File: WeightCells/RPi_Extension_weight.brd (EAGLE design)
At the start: 80 x 50 mm, 29 parts, among them U1 AD7730BRUZ, U2 AD7730BRUZ, U3 AD7730BRUZ, U4 AD7730BRUZ, U5 AD7730BRUZ, U6 AD7730BRUZ, U7 AD7730BRUZ, U8 AD7730BRUZ, U9 STM32F103RCT6

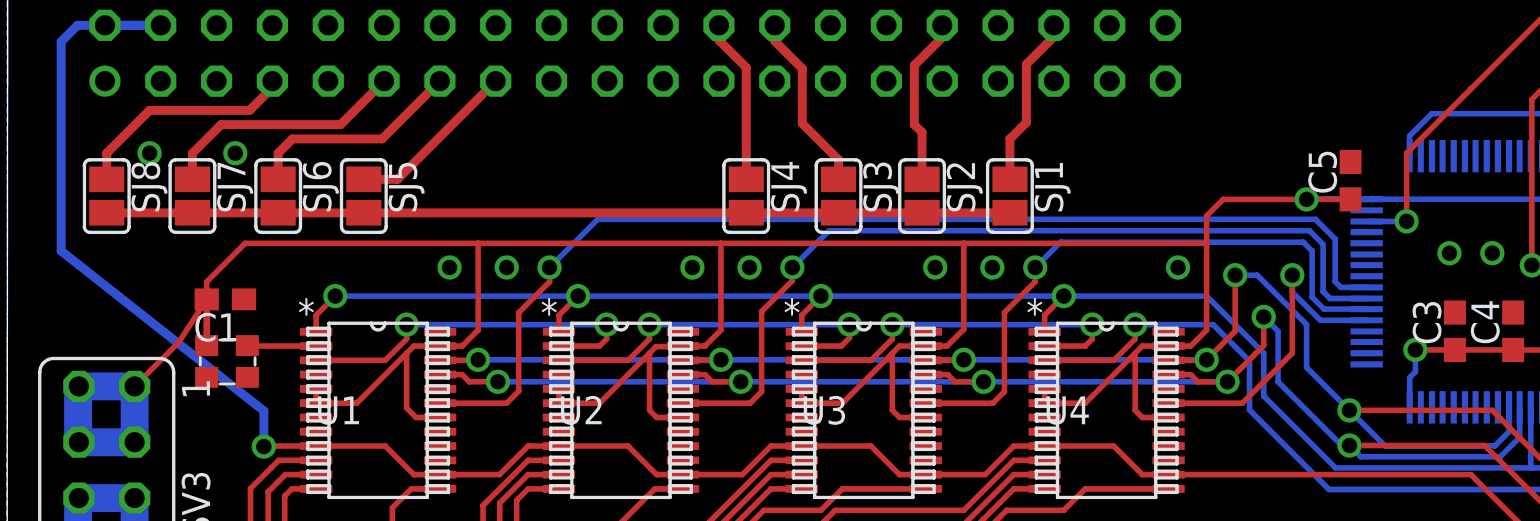
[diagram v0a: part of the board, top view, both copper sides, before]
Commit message: fixed grounding error and missplaced trace
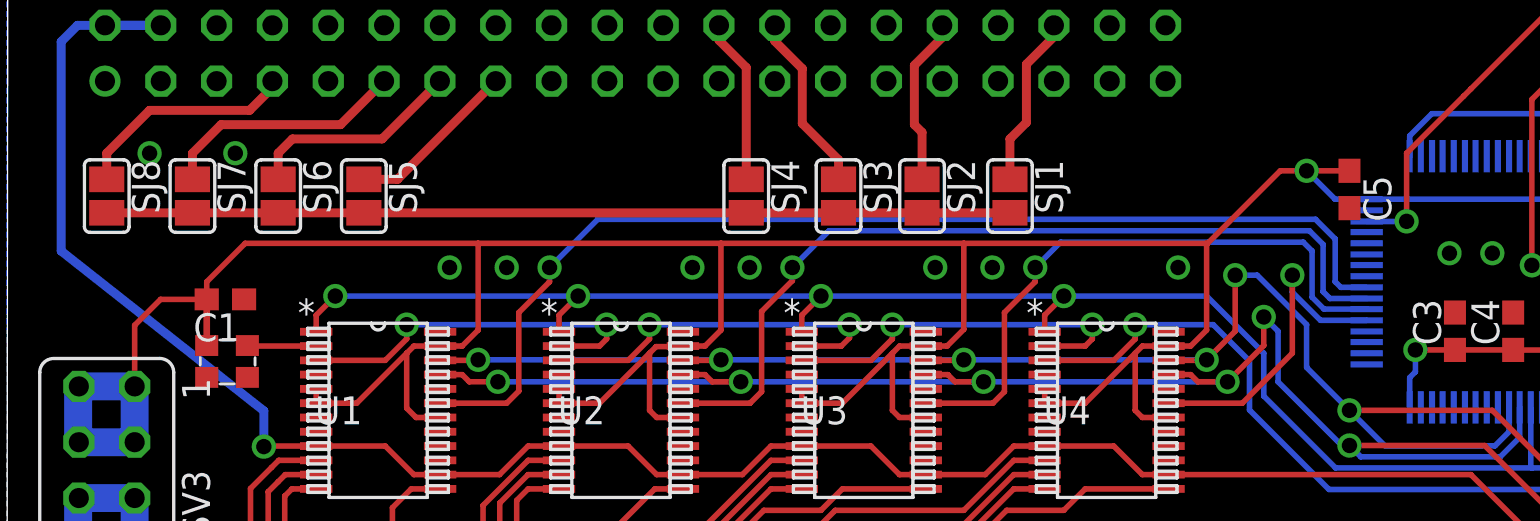
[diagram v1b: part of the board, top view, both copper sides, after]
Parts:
- moved C5 0.40 mm to (61.1, 35.4), turned to 270 degrees
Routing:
- net DVCC: track 280.9 -> 282.5 mm
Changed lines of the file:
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@@
 <grid distance="0.65" unitdist="mm" unit="mm" style="lines" multiple="1" display="yes" altdistance="0.05" altunitdist="mm" altunit="mm"/>
 <layers>
-<layer number="1" name="Top" color="4" fill="1" visible="no" active="yes"/>
+<layer number="1" name="Top" color="4" fill="1" visible="yes" active="yes"/>
 <layer number="2" name="Route2" color="1" fill="3" visible="no" active="no"/>
 <layer number="3" name="Route3" color="4" fill="3" visible="no" active="no"/>
@@
 <element name="C3" library="rcl" package="C0603" value="" x="65.9" y="28.95" rot="R90"/>
 <element name="C4" library="rcl" package="C0603" value="" x="68.55" y="28.95" rot="R90"/>
-<element name="C5" library="rcl" package="C0603" value="" x="61.15" y="35.8" rot="R90"/>
+<element name="C5" library="rcl" package="C0603" value="" x="61.1" y="35.4" rot="R270"/>
 <element name="C6" library="rcl" package="C0603" value="" x="77.3" y="35.8" rot="MR90"/>
 <element name="SV4" library="con-lstb" package="MA03-2" value="" x="75.4" y="42.9" rot="R90">
@@
 <contactref element="U8" pad="4"/>
 <contactref element="U8" pad="15"/>
-<wire x1="61.885" y1="34.4512" x2="61.15" y2="36.65" width="0" layer="19" extent="1-16"/>
 </signal>
 <signal name="DVCC">
@@
 <wire x1="10.85" y1="32.95" x2="9.1" y2="31.2" width="0.254" layer="1"/>
 <wire x1="9.1" y1="31.2" x2="9.1" y2="30.4" width="0.254" layer="1"/>
-<wire x1="9.1" y1="30.4" x2="7.83" y2="28.45" width="0.254" layer="1"/>
-<wire x1="7.83" y1="28.45" x2="5.82" y2="26.44" width="0.254" layer="1"/>
 <contactref element="U5" pad="23"/>
 <contactref element="U5" pad="5"/>
@@
 <wire x1="64.1" y1="27.1" x2="63.8408" y2="26.8408" width="0.254" layer="16"/>
 <wire x1="76.67" y1="40.36" x2="76.67" y2="38.32" width="0.254" layer="16"/>
-<wire x1="61.885" y1="34.9592" x2="59.1592" y2="34.9592" width="0.254" layer="16"/>
-<wire x1="59.1592" y1="34.9592" x2="59.15" y2="34.95" width="0.254" layer="16"/>
-<via x="59.15" y="34.95" extent="1-16" drill="0.7"/>
-<wire x1="59.15" y1="34.95" x2="61.15" y2="34.95" width="0.254" layer="1"/>
-<wire x1="54.6" y1="32.9" x2="54.6" y2="34.2" width="0.254" layer="1"/>
-<wire x1="54.6" y1="34.2" x2="55.35" y2="34.95" width="0.254" layer="1"/>
-<wire x1="55.35" y1="34.95" x2="59.15" y2="34.95" width="0.254" layer="1"/>
+<via x="59.15" y="36.25" extent="1-16" drill="0.7"/>
+<wire x1="59.15" y1="36.25" x2="61.1" y2="36.25" width="0.254" layer="1"/>
+<wire x1="59.15" y1="36.25" x2="57.95" y2="36.25" width="0.254" layer="1"/>
+<wire x1="57.95" y1="36.25" x2="54.6" y2="32.9" width="0.254" layer="1"/>
 <wire x1="54.6" y1="29" x2="54.6" y2="32.9" width="0.254" layer="1"/>
 <wire x1="54.55" y1="32.95" x2="54.6" y2="32.9" width="0.254" layer="1"/>
@@
 <wire x1="75.8106" y1="28.9394" x2="76.45" y2="28.3" width="0.254" layer="16"/>
 <wire x1="76.45" y1="28.3" x2="77.3" y2="28.3" width="0.254" layer="16"/>
+<wire x1="5.82" y1="26.44" x2="5.82" y2="29.22" width="0.254" layer="1"/>
+<wire x1="5.82" y1="29.22" x2="7" y2="30.4" width="0.254" layer="1"/>
+<wire x1="9.1" y1="30.4" x2="7" y2="30.4" width="0.254" layer="1"/>
+<wire x1="61.885" y1="34.9592" x2="60.4408" y2="34.9592" width="0.254" layer="16"/>
+<wire x1="60.4408" y1="34.9592" x2="59.15" y2="36.25" width="0.254" layer="16"/>
 </signal>
 <signal name="MISO">

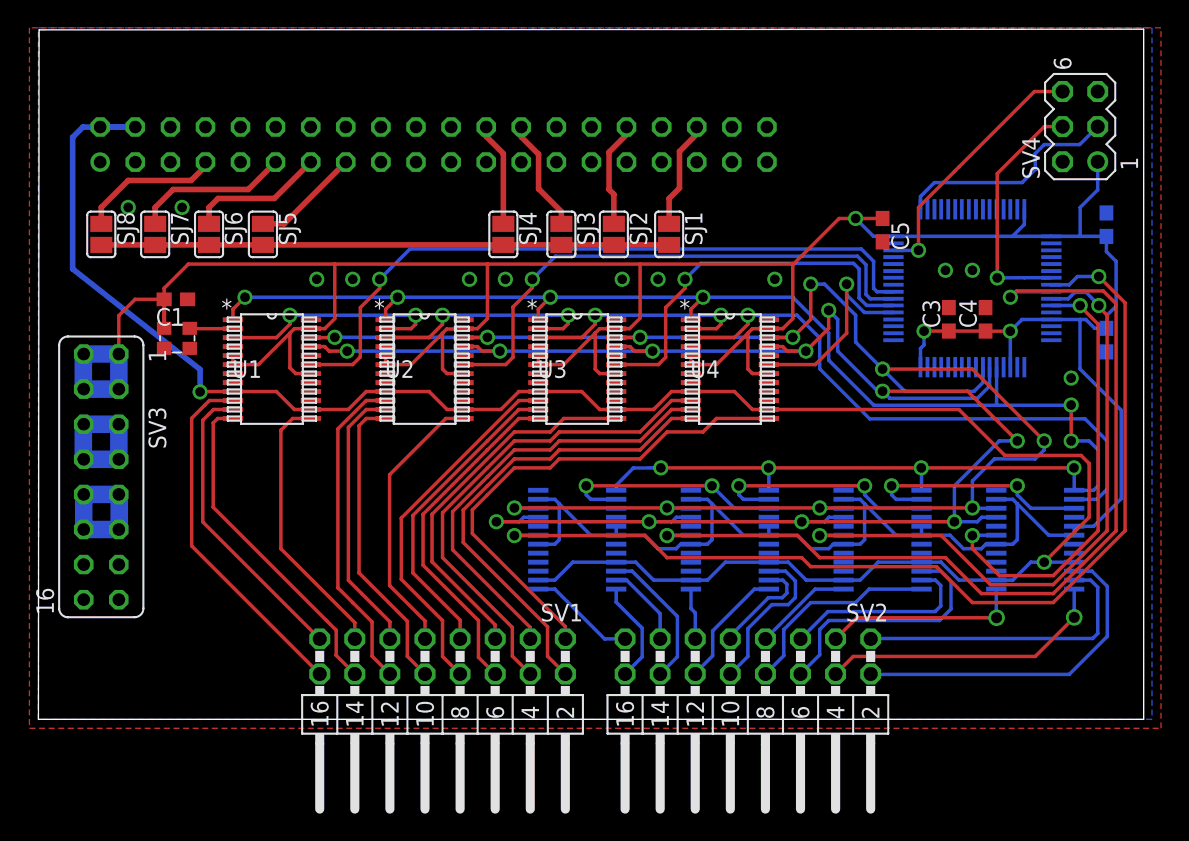
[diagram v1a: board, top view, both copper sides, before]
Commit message: added crystal and revisited layout
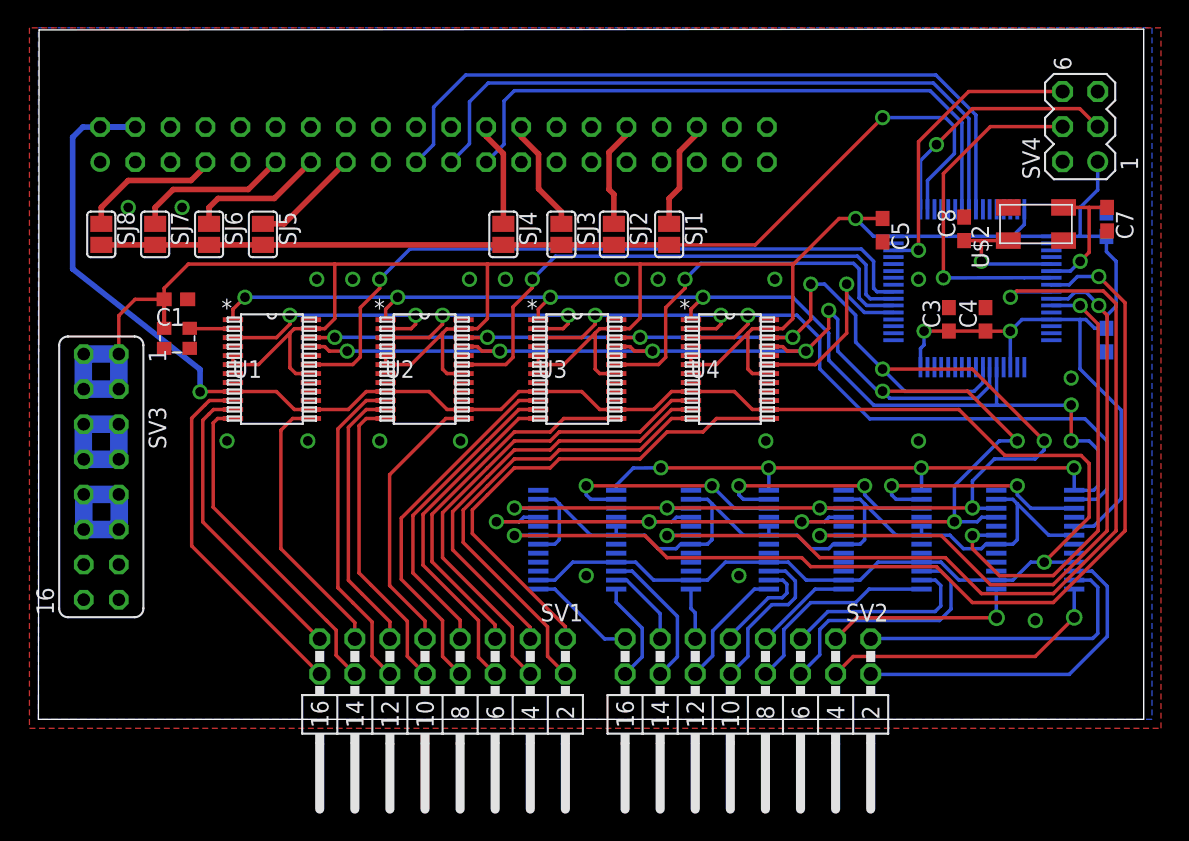
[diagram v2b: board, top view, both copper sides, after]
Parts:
- added C7, C8: 33pf, rcl:C0603
- added U$2: ABM3B, ABM3B:ABM3B
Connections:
- new net N$2: C8.1, U$2.1, U9.5
- new net N$3: C7.1, U$2.3, U9.6
- net GND: now also C7.2, C8.2, U$2.2, U$2.4
- net MISO: now also U9.56
- net MOSI: now also U9.57
- net SCLK: now also U9.55
- net SS_STACK: now also U9.50
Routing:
- net MOSI: track 0.00 -> 52.7 mm
- net MISO: track 0.00 -> 49.3 mm
- net SCLK: track 0.00 -> 45.6 mm
- net SS_STACK: track 41.1 -> 72.6 mm, vias 0 -> 1
- net N$2: track 0.00 -> 9.85 mm, vias 0 -> 1
- net N$3: track 0.00 -> 9.70 mm, vias 0 -> 1
- net NRST: track 17.6 -> 25.4 mm
- net SWDIO: track 18.8 -> 21.6 mm
- net SWDCLK: track 16.5 -> 18.5 mm, vias 0 -> 1
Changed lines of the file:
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@@
 <element name="U7" library="AD7730BRUZ" package="RU_24" value="AD7730BRUZ" x="50.05" y="13" rot="MR0"/>
 <element name="U8" library="AD7730BRUZ" package="RU_24" value="AD7730BRUZ" x="39" y="13" rot="MR0"/>
+<element name="U$2" library="ABM3B" package="ABM3B" value="ABM3B" x="70.2" y="37.05"/>
+<element name="C7" library="rcl" package="C0603" value="33pf" x="77.35" y="36.2" rot="R270"/>
+<element name="C8" library="rcl" package="C0603" value="33pf" x="67" y="35.5" rot="R90"/>
 </elements>
 <signals>
@@
 <contactref element="SV4" pad="2"/>
 <contactref element="SV4" pad="5"/>
-<via x="65.65" y="32.5" extent="1-16" drill="0.7"/>
-<via x="67.6" y="32.5" extent="1-16" drill="0.7"/>
+<via x="63.7" y="31.85" extent="1-16" drill="0.7"/>
 <contactref element="U1" pad="4"/>
 <contactref element="U1" pad="15"/>
@@
 <contactref element="U8" pad="4"/>
 <contactref element="U8" pad="15"/>
+<via x="19.5" y="20.15" extent="1-16" drill="0.7"/>
+<via x="30.55" y="20.15" extent="1-16" drill="0.7"/>
+<via x="24.7" y="20.15" extent="1-16" drill="0.7"/>
+<via x="13.65" y="20.15" extent="1-16" drill="0.7"/>
+<via x="52.65" y="20.15" extent="1-16" drill="0.7"/>
+<via x="63.7" y="20.15" extent="1-16" drill="0.7"/>
+<via x="72.15" y="7.15" extent="1-16" drill="0.7"/>
+<contactref element="U$2" pad="2"/>
+<contactref element="U$2" pad="4"/>
+<contactref element="C7" pad="2"/>
+<contactref element="C8" pad="2"/>
+<via x="39.65" y="10.4" extent="1-16" drill="0.7"/>
+<via x="50.7" y="10.4" extent="1-16" drill="0.7"/>
 </signal>
 <signal name="DVCC">
@@
 <signal name="MISO">
 <contactref element="SV5" pad="21"/>
+<contactref element="U9" pad="56"/>
+<wire x1="67.346" y1="36.915" x2="67.346" y2="43.4831375" width="0.254" layer="16"/>
+<wire x1="67.346" y1="43.4831375" x2="64.7755875" y2="46.05355" width="0.254" layer="16"/>
+<wire x1="64.7755875" y1="46.05355" x2="32.55699375" y2="46.05355" width="0.254" layer="16"/>
+<wire x1="32.55699375" y1="46.05355" x2="31.2" y2="44.69655625" width="0.254" layer="16"/>
+<wire x1="31.2" y1="44.69655625" x2="31.2" y2="41.66" width="0.254" layer="16"/>
+<wire x1="31.2" y1="41.66" x2="29.87" y2="40.33" width="0.254" layer="16"/>
 </signal>
 <signal name="SCLK">
 <contactref element="SV5" pad="23"/>
+<contactref element="U9" pad="55"/>
+<wire x1="66.838" y1="36.915" x2="66.838" y2="43.201371875" width="0.254" layer="16"/>
+<wire x1="66.838" y1="43.201371875" x2="64.537046875" y2="45.502325" width="0.254" layer="16"/>
+<wire x1="64.537046875" y1="45.502325" x2="34.452325" y2="45.502325" width="0.254" layer="16"/>
+<wire x1="34.452325" y1="45.502325" x2="33.7" y2="44.75" width="0.254" layer="16"/>
+<wire x1="33.7" y1="44.75" x2="33.7" y2="41.62" width="0.254" layer="16"/>
+<wire x1="33.7" y1="41.62" x2="32.41" y2="40.33" width="0.254" layer="16"/>
 </signal>
 <signal name="VDD">
@@
 <signal name="MOSI">
 <contactref element="SV5" pad="19"/>
+<contactref element="U9" pad="57"/>
+<wire x1="67.854" y1="36.915" x2="67.854" y2="43.73674375" width="0.254" layer="16"/>
+<wire x1="67.854" y1="43.73674375" x2="64.957425" y2="46.63331875" width="0.254" layer="16"/>
+<wire x1="64.957425" y1="46.63331875" x2="30.923434375" y2="46.63331875" width="0.254" layer="16"/>
+<wire x1="30.923434375" y1="46.63331875" x2="28.6" y2="44.309884375" width="0.254" layer="16"/>
+<wire x1="28.6" y1="44.309884375" x2="28.6" y2="41.6" width="0.254" layer="16"/>
+<wire x1="28.6" y1="41.6" x2="27.33" y2="40.33" width="0.254" layer="16"/>
 </signal>
 <signal name="N$20">
@@
 <via x="63.7" y="33.95" extent="1-16" drill="0.7"/>
 <contactref element="SV4" pad="6"/>
-<wire x1="74.13" y1="45.44" x2="72.09" y2="45.44" width="0.254" layer="1"/>
-<wire x1="72.09" y1="45.44" x2="66.625" y2="39.975" width="0.254" layer="1"/>
-<wire x1="66.625" y1="39.975" x2="66.3" y2="39.65" width="0.254" layer="1"/>
-<wire x1="63.7" y1="33.95" x2="63.7" y2="37.05" width="0.254" layer="1"/>
-<wire x1="63.7" y1="37.05" x2="66.3" y2="39.65" width="0.254" layer="1"/>
+<wire x1="74.13" y1="45.44" x2="67.334775" y2="45.44" width="0.254" layer="1"/>
+<wire x1="67.334775" y1="45.44" x2="63.7" y2="41.805225" width="0.254" layer="1"/>
+<wire x1="63.7" y1="41.805225" x2="63.7" y2="33.95" width="0.254" layer="1"/>
 </signal>
 <signal name="SWDCLK">
 <contactref element="SV4" pad="3"/>
 <contactref element="U9" pad="49"/>
-<wire x1="63.8408" y1="36.915" x2="63.8408" y2="37.8408" width="0.254" layer="16"/>
-<wire x1="63.8408" y1="37.8408" x2="64.85" y2="38.85" width="0.254" layer="16"/>
-<wire x1="72.15" y1="39.80344375" x2="72.15" y2="40.95" width="0.254" layer="16"/>
-<wire x1="72.15" y1="40.95" x2="72.8" y2="41.6" width="0.254" layer="16"/>
-<wire x1="72.8" y1="41.6" x2="75.37" y2="41.6" width="0.254" layer="16"/>
-<wire x1="75.37" y1="41.6" x2="76.67" y2="42.9" width="0.254" layer="16"/>
-<wire x1="64.85" y1="38.85" x2="71.19655625" y2="38.85" width="0.254" layer="16"/>
-<wire x1="71.19655625" y1="38.85" x2="72.15" y2="39.80344375" width="0.254" layer="16"/>
+<wire x1="63.8408" y1="36.915" x2="63.8408" y2="40.4408" width="0.254" layer="16"/>
+<wire x1="63.8408" y1="40.4408" x2="65" y2="41.6" width="0.254" layer="16"/>
+<via x="65" y="41.6" extent="1-16" drill="0.7"/>
+<wire x1="65" y1="41.6" x2="67.6" y2="44.2" width="0.254" layer="1"/>
+<wire x1="67.6" y1="44.2" x2="75.37" y2="44.2" width="0.254" layer="1"/>
+<wire x1="75.37" y1="44.2" x2="76.67" y2="42.9" width="0.254" layer="1"/>
 </signal>
 <signal name="NRST">
 <contactref element="U9" pad="7"/>
-<wire x1="71.362" y1="31.962" x2="69.4" y2="31.95" width="0.254" layer="16"/>
-<via x="69.4" y="31.95" extent="1-16" drill="0.7"/>
+<wire x1="71.362" y1="31.962" x2="65.5" y2="31.95" width="0.254" layer="16"/>
+<via x="65.5" y="31.95" extent="1-16" drill="0.7"/>
 <wire x1="73.315" y1="31.962" x2="71.362" y2="31.962" width="0.254" layer="16"/>
 <contactref element="SV4" pad="4"/>
-<wire x1="74.13" y1="42.9" x2="72.8" y2="42.9" width="0.254" layer="1"/>
-<wire x1="72.8" y1="42.9" x2="69.4" y2="39.5" width="0.254" layer="1"/>
-<wire x1="69.4" y1="31.95" x2="69.4" y2="39.5" width="0.254" layer="1"/>
+<wire x1="65.5" y1="31.95" x2="65.5" y2="39.5" width="0.254" layer="1"/>
+<wire x1="74.13" y1="42.9" x2="68.9" y2="42.9" width="0.254" layer="1"/>
+<wire x1="68.9" y1="42.9" x2="65.5" y2="39.5" width="0.254" layer="1"/>
 </signal>
 <signal name="SS1">
@@
 <wire x1="52.8694" y1="21.775" x2="49.075" y2="21.775" width="0.254" layer="1"/>
 <wire x1="49.075" y1="21.775" x2="48.1" y2="20.8" width="0.254" layer="1"/>
-<wire x1="48.1" y1="20.8" x2="45.5" y2="20.8" width="0.254" layer="1"/>
 <wire x1="45.5" y1="20.8" x2="43.55" y2="18.85" width="0.254" layer="1"/>
 <wire x1="43.55" y1="18.85" x2="37.7" y2="18.85" width="0.254" layer="1"/>
@@
 <wire x1="31.40513125" y1="13.44486875" x2="38.14" y2="6.71" width="0.254" layer="1"/>
 <wire x1="38.14" y1="5.82" x2="38.14" y2="6.71" width="0.254" layer="1"/>
+<wire x1="48.1" y1="20.8" x2="45.5" y2="20.8" width="0.254" layer="1"/>
 </signal>
 <signal name="U4_AIN1_+">
@@
 <wire x1="33.65" y1="34.35" x2="33.65" y2="34.338" width="0.4064" layer="1"/>
 <wire x1="16.25" y1="34.338" x2="33.65" y2="34.338" width="0.4064" layer="1"/>
+<contactref element="U9" pad="50"/>
+<wire x1="64.3488" y1="36.915" x2="64.3488" y2="38.9988" width="0.254" layer="16"/>
+<wire x1="64.3488" y1="38.9988" x2="66.3" y2="40.95" width="0.254" layer="16"/>
+<wire x1="66.3" y1="40.95" x2="66.3" y2="42.9" width="0.254" layer="16"/>
+<wire x1="66.3" y1="42.9" x2="65.65" y2="43.55" width="0.254" layer="16"/>
+<wire x1="65.65" y1="43.55" x2="61.1" y2="43.55" width="0.254" layer="16"/>
+<via x="61.1" y="43.55" extent="1-16" drill="0.7"/>
+<wire x1="61.1" y1="43.55" x2="51.888" y2="34.338" width="0.254" layer="1"/>
+<wire x1="45.65" y1="34.338" x2="51.888" y2="34.338" width="0.254" layer="1"/>
 </signal>
 <signal name="U2_MCLK_OUT">
@@
 <wire x1="56.225" y1="9.425" x2="52.62" y2="5.82" width="0.254" layer="16"/>
 </signal>
+<signal name="N$2">
+<contactref element="U$2" pad="1"/>
+<contactref element="U9" pad="5"/>
+<contactref element="C8" pad="1"/>
+<wire x1="73.315" y1="32.9526" x2="68.4474" y2="32.9526" width="0.254" layer="16"/>
+<wire x1="68.4474" y1="32.9526" x2="68.25" y2="33.15" width="0.254" layer="16"/>
+<via x="68.25" y="33.15" extent="1-16" drill="0.7"/>
+<wire x1="68.25" y1="33.15" x2="68.25" y2="34.65" width="0.254" layer="1"/>
+<wire x1="68.25" y1="34.65" x2="67.7" y2="34.65" width="0.254" layer="1"/>
+<wire x1="67.7" y1="34.65" x2="67" y2="34.65" width="0.254" layer="1"/>
+<wire x1="70.2" y1="34.65" x2="68.25" y2="34.65" width="0.254" layer="1"/>
+</signal>
+<signal name="N$3">
+<contactref element="U$2" pad="3"/>
+<contactref element="U9" pad="6"/>
+<contactref element="C7" pad="1"/>
+<wire x1="73.315" y1="32.4446" x2="74.6946" y2="32.4446" width="0.254" layer="16"/>
+<wire x1="74.6946" y1="32.4446" x2="75.4" y2="33.15" width="0.254" layer="16"/>
+<via x="75.4" y="33.15" extent="1-16" drill="0.7"/>
+<wire x1="75.4" y1="33.15" x2="76.05" y2="33.8" width="0.254" layer="1"/>
+<wire x1="76.05" y1="37.05" x2="74.2" y2="37.05" width="0.254" layer="1"/>
+<wire x1="76.05" y1="33.8" x2="76.05" y2="37.05" width="0.254" layer="1"/>
+<wire x1="77.35" y1="37.05" x2="76.05" y2="37.05" width="0.254" layer="1"/>
+</signal>
 </signals>

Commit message: vias revisited
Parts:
- moved C3 0.25 mm to (65.7, 28.9)
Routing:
- net SS7: track 65.6 -> 64.6 mm
- net SCLK: track 45.6 -> 45.0 mm
- net MISO: track 49.3 -> 48.7 mm

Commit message: vias revisited
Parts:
- C2, C3, C4, C5, C6: value (none) -> 100nf
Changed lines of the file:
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@@
 <element name="U$1" library="kc2520b_c1" package="KC2520B-C1" value="KC2520B-C1" x="9.1" y="28.3"/>
 <element name="C1" library="rcl" package="C0603" value="0.1uf" x="9.95" y="30.4" rot="R180"/>
-<element name="C2" library="rcl" package="C0603" value="" x="77.3" y="27.45" rot="MR90"/>
-<element name="C3" library="rcl" package="C0603" value="" x="65.65" y="28.95" rot="R90"/>
-<element name="C4" library="rcl" package="C0603" value="" x="68.55" y="28.95" rot="R90"/>
-<element name="C5" library="rcl" package="C0603" value="" x="61.1" y="35.4" rot="R270"/>
-<element name="C6" library="rcl" package="C0603" value="" x="77.3" y="35.8" rot="MR90"/>
+<element name="C2" library="rcl" package="C0603" value="100nf" x="77.3" y="27.45" rot="MR90"/>
+<element name="C3" library="rcl" package="C0603" value="100nf" x="65.65" y="28.95" rot="R90"/>
+<element name="C4" library="rcl" package="C0603" value="100nf" x="68.55" y="28.95" rot="R90"/>
+<element name="C5" library="rcl" package="C0603" value="100nf" x="61.1" y="35.4" rot="R270"/>
+<element name="C6" library="rcl" package="C0603" value="100nf" x="77.3" y="35.8" rot="MR90"/>
 <element name="SV4" library="con-lstb" package="MA03-2" value="" x="75.4" y="42.9" rot="R90">
 <attribute name="OC_NEWARK" value="unknown" x="75.4" y="42.9" size="1.778" layer="27" rot="R90" display="off"/>
